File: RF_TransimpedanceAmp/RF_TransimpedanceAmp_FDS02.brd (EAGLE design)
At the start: 76.2 x 50.8 mm, 39 parts, among them IC1 LT1964-5, IC2 OPA847, IC3 PMA-5452, IC4 ADM7150ARDZ-3.0, IC5 ADM7150ARDZ-5.0, IC6 PMA-5452

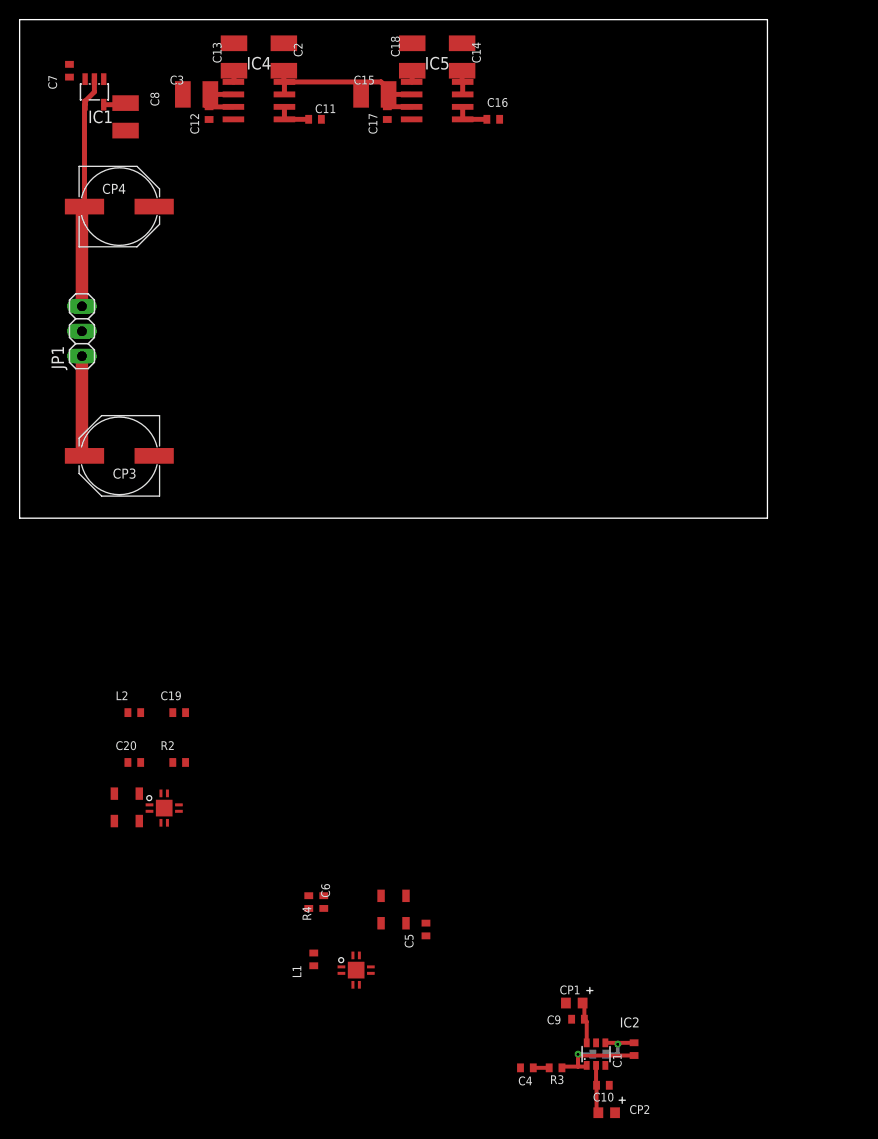
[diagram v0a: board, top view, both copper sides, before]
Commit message: First draft schematic and layout for FDS02 transimpedance amplifier.
* Low transimpedance gain, followed by low-noise RF amplifier.
* FDS02 is FC-connectorized, mount on bottom of board and standoff from front panel.

TODO:
* Remove -5V supply?
* Compare OPA847 vs some FET-input op amp
* Filtering on PD bias voltage?
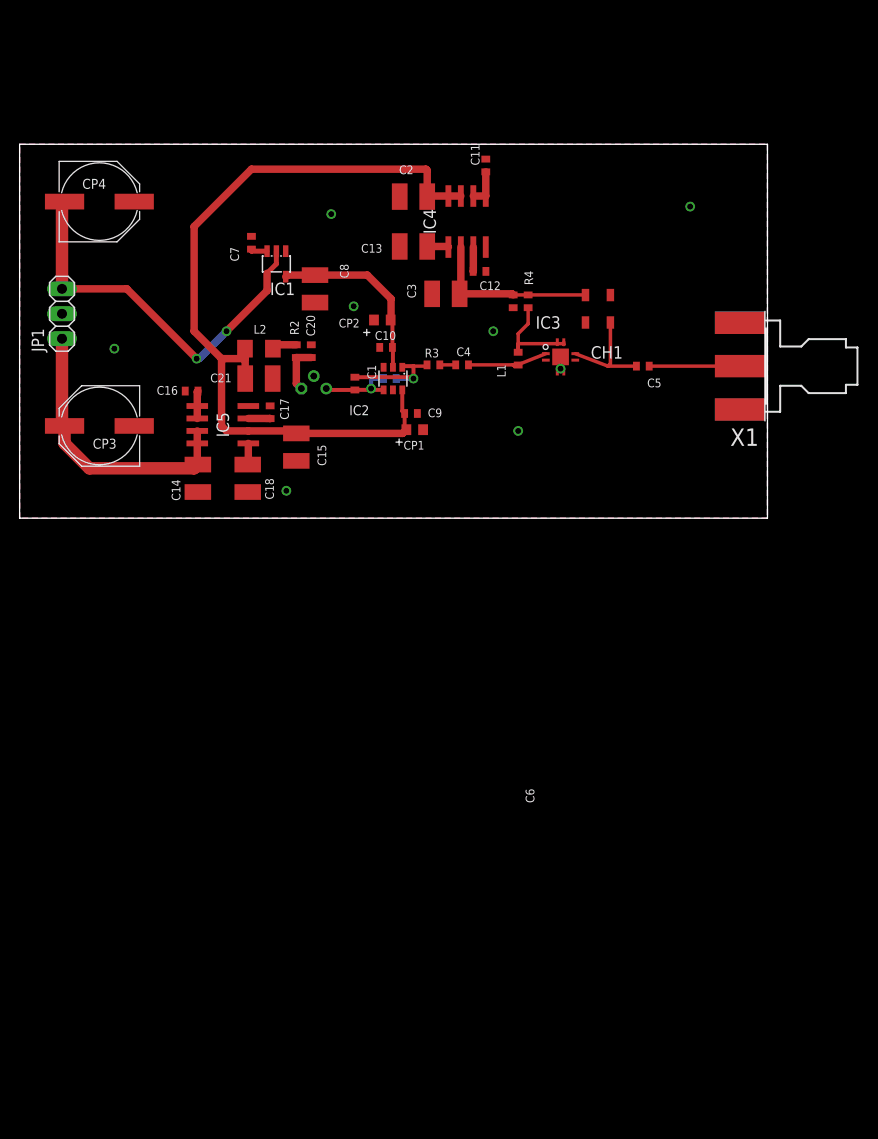
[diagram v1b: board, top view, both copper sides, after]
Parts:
- removed C19: 100nF, rlc-jqi:0402
- removed CH2: TCCH-80, rf-jqi:GU1604
- removed IC6: PMA-5452, rf-jqi:DQ849
- added C21: 10uF, rlc-jqi:1210
- added PD1: FDS02, semiconductor-jqi:FDS02
- added X1: SMAJ502, connector-jqi:SMA-EDGE
- L2: value 390nH -> Ferrite Bead; device rlc-jqi:0402 -> rlc-jqi:1206
- moved CP2 83.9 mm to (37.0, 20.2), turned to 0 degrees
- moved C10 78.4 mm to (37.3, 17.4), turned to 0 degrees
- moved C1 73.5 mm to (34.2, 13.7), turned to 270 degrees
- moved R3 72.7 mm to (42.2, 15.6), turned to 0 degrees
- moved R1 72.1 mm to (37.7, 14.2), turned to 180 degrees
- moved C4 71.9 mm to (45.1, 15.6), turned to 180 degrees
- moved IC2 71.4 mm to (39.0, 14.2), turned to 180 degrees
- moved C6 64.7 mm to (50.3, 22.1)
- moved CH1 64.7 mm to (58.9, 21.3)
- moved IC3 64.7 mm to (55.1, 15.5)
- moved L1 64.7 mm to (50.8, 16.3)
- moved R4 64.7 mm to (51.8, 22.1)
- moved C9 64.0 mm to (39.9, 10.7), turned to 180 degrees
- moved C5 61.5 mm to (63.5, 15.5), turned to 180 degrees
- moved CP1 60.6 mm to (40.3, 9.02), turned to 0 degrees
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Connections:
- removed net N$11: IC6.P$7, L2.2, R2.1
- net +3V: no longer C20.1, CH2.P$3, R2.2
- net +5V: now also C21.2, L2.2
- net GND: now also C20.1, C21.1, X1.G@1, X1.G@2, X1.G@3, X1.G@4; no longer C20.2, IC6.P$GND
- net N$2: now also PD1.P$3
- net N$5: now also L2.1, R2.2; no longer C19.2, CH2.P$1, IC6.P$6
- net N$7: now also X1.1
- net N$8: now also C20.2, PD1.P$1, R2.1; no longer C19.1
- net RFPD: no longer IC6.P$1, L2.1
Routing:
- net +5V: track 20.4 -> 82.8 mm
- net -15V: track 23.7 -> 40.5 mm, vias 0 -> 2
- net +15V: track 12.7 -> 29.0 mm
- net +3V: track 2.35 -> 17.7 mm
- net -5V: track 7.17 -> 18.9 mm
- net N$6: track 0.00 -> 11.0 mm
- net N$9: track 0.00 -> 10.7 mm
- net N$7: track 0.00 -> 9.23 mm
- net RFPD: track 0.00 -> 8.69 mm
- net N$8: track 0.00 -> 4.89 mm
- net N$2: track 5.33 -> 8.40 mm
- net N$5: track 0.00 -> 2.78 mm
- net N$10: track 0.00 -> 1.80 mm
- net N$14: track 1.16 -> 2.18 mm
- net N$19: track 1.16 -> 2.18 mm
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- added copper zone on layer 1, net GND
- added copper zone on layer 16, net GND
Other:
- board size 76.2 x 50.8 mm -> 76.2 x 38.1 mm

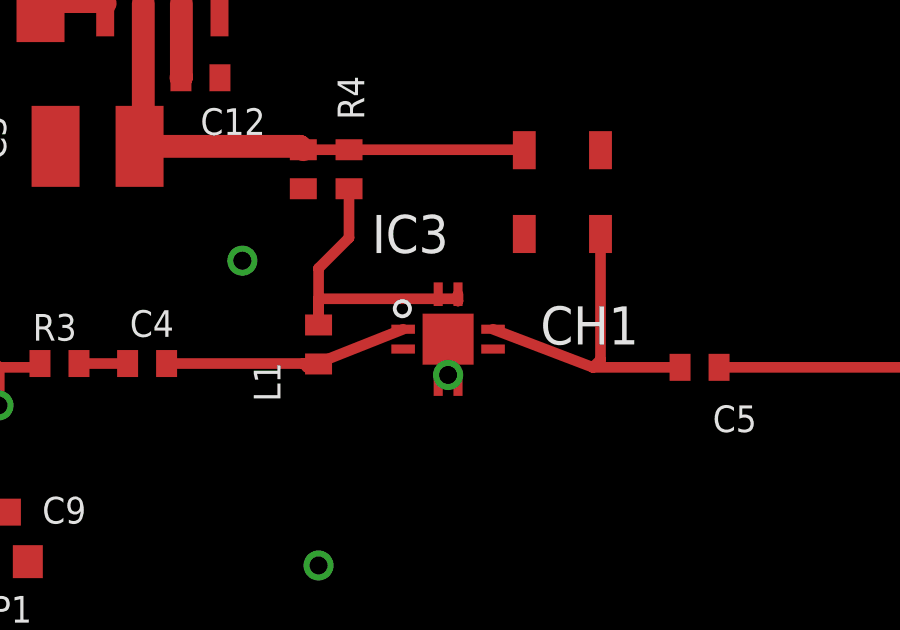
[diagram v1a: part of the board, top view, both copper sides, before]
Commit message: Minor tweaks to schematic notes; need to check 50 ohm trace width then ready to print.
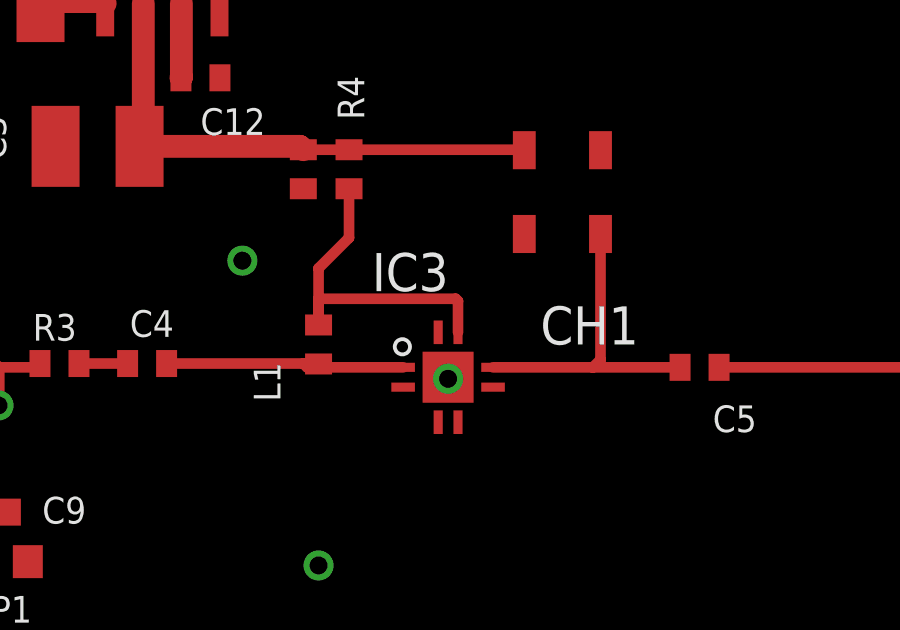
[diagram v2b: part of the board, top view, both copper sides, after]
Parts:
- moved IC3 1.27 mm to (55.1, 14.2)
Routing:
- net N$9: track 10.7 -> 11.6 mm
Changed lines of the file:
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@@
 <setting verticaltext="up"/>
 </settings>
-<grid distance="0.01" unitdist="inch" unit="inch" style="lines" multiple="1" display="yes" altdistance="0.025" altunitdist="inch" altunit="inch"/>
+<grid distance="0.005" unitdist="inch" unit="inch" style="lines" multiple="1" display="yes" altdistance="0.025" altunitdist="inch" altunit="inch"/>
 <layers>
 <layer number="1" name="Top" color="4" fill="1" visible="yes" active="yes"/>
@@
 </autorouter>
 <elements>
-<element name="IC3" library="rf-jqi" package="DQ849" value="PMA-5452" x="55.118" y="15.494"/>
+<element name="IC3" library="rf-jqi" package="DQ849" value="PMA-5452" x="55.118" y="14.224"/>
 <element name="C5" library="rlc-jqi" package="0402" value="100nF" x="63.5" y="15.494" rot="R180"/>
 <element name="CH1" library="rf-jqi" package="GU1604" value="TCCH-80" x="58.928" y="21.336" rot="R180"/>
@@
 <via x="48.26" y="19.05" extent="1-16" drill="0.6"/>
 <via x="50.8" y="8.89" extent="1-16" drill="0.6"/>
-<via x="55.118" y="15.24" extent="1-16" drill="0.6"/>
+<via x="55.118" y="15.113" extent="1-16" drill="0.6"/>
 <via x="68.326" y="31.75" extent="1-16" drill="0.6"/>
 <via x="31.75" y="30.988" extent="1-16" drill="0.6"/>
@@
 <contactref element="C21" pad="1"/>
 <via x="34.036" y="21.59" extent="1-16" drill="0.6"/>
-<wire x1="55.118" y1="16.4338" x2="55.118" y2="15.24" width="0" layer="19" extent="1-1"/>
 </signal>
 <signal name="+5V">
@@
 <contactref element="C5" pad="2"/>
 <contactref element="CH1" pad="P$1"/>
-<wire x1="56.6166" y1="16.764" x2="59.944" y2="15.494" width="0.3556" layer="1"/>
+<wire x1="56.6166" y1="15.494" x2="59.944" y2="15.494" width="0.3556" layer="1"/>
 <wire x1="59.944" y1="15.494" x2="62.85" y2="15.494" width="0.3556" layer="1"/>
 <wire x1="60.198" y1="19.939" x2="60.198" y2="15.748" width="0.3556" layer="1"/>
@@
 <contactref element="R4" pad="1"/>
 <contactref element="IC3" pad="P$7"/>
-<wire x1="55.4482" y1="17.9324" x2="55.4482" y2="17.7038" width="0.3556" layer="1"/>
+<wire x1="55.4482" y1="16.6624" x2="55.4482" y2="17.7038" width="0.3556" layer="1"/>
 <wire x1="55.4482" y1="17.7038" x2="55.372" y2="17.78" width="0.3556" layer="1"/>
 <wire x1="55.372" y1="17.78" x2="50.8" y2="17.78" width="0.3556" layer="1"/>
@@
 <wire x1="50.292" y1="15.621" x2="50.785" y2="15.621" width="0.3556" layer="1"/>
 <wire x1="50.785" y1="15.621" x2="50.8" y2="15.606" width="0.3556" layer="1"/>
-<wire x1="53.6194" y1="16.764" x2="50.419" y2="15.494" width="0.3556" layer="1"/>
+<wire x1="53.6194" y1="15.494" x2="50.419" y2="15.494" width="0.3556" layer="1"/>
 <wire x1="50.419" y1="15.494" x2="50.292" y2="15.621" width="0.3556" layer="1"/>
 </signal>
